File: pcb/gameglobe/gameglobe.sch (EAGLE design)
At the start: 14 parts

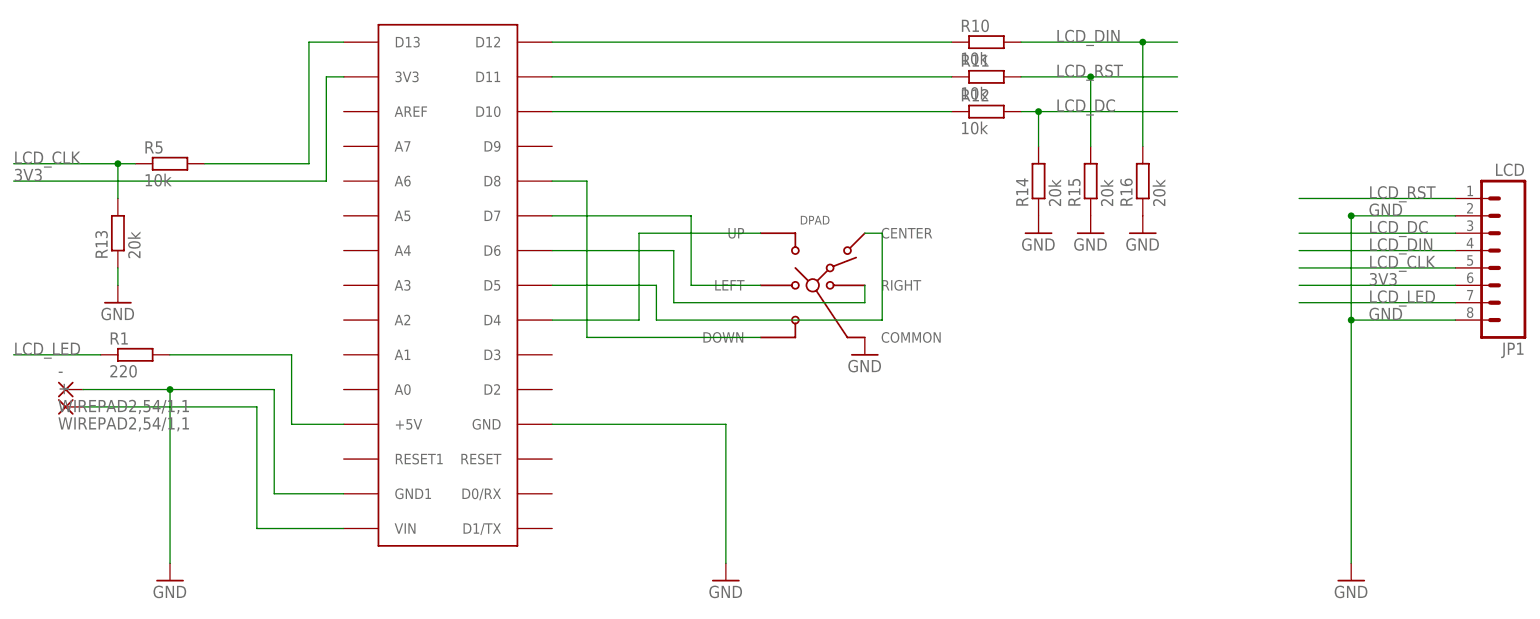
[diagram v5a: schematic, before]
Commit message: Fix and add own arduino Improve silkscreen texts
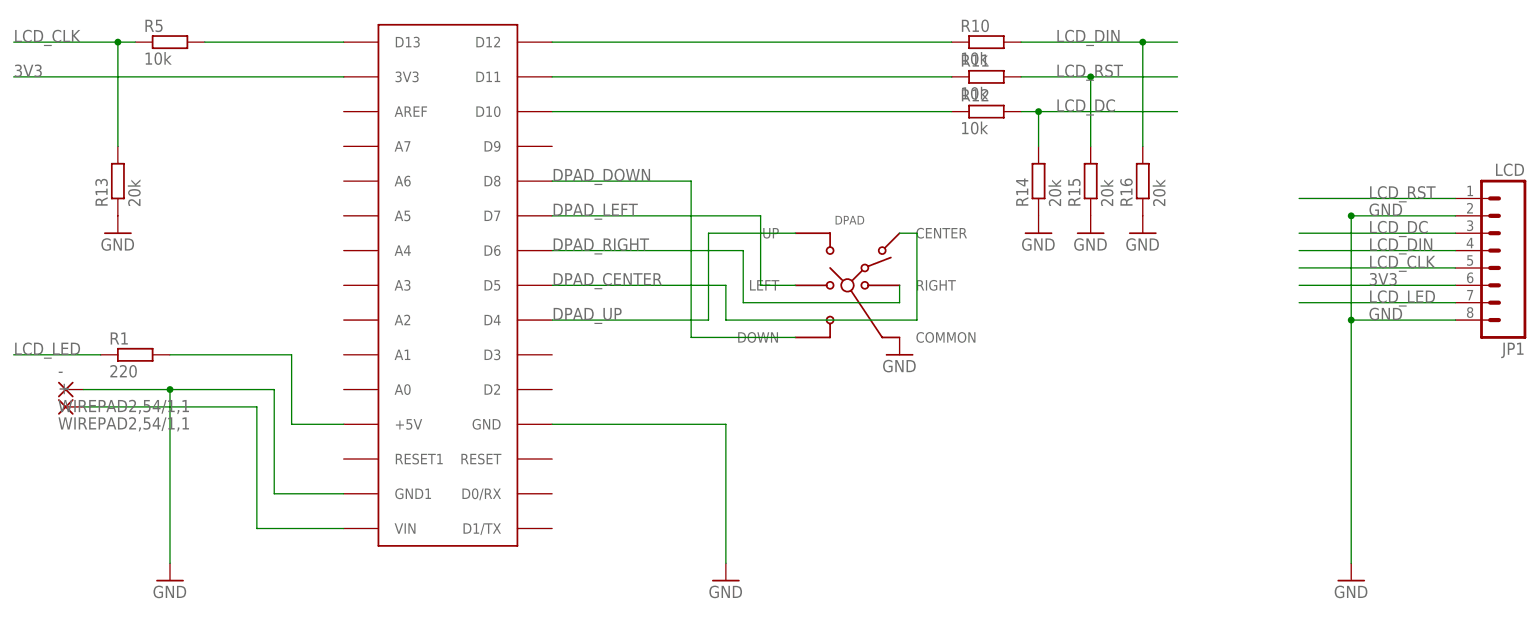
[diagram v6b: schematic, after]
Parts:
- removed U$5: ARDUINONANO, jet-lib:ARDUINONANO
- added ARDUINO_NANO: ARDUINONANO, arduino_nano:ARDUINONANO
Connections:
- removed net N$5: DPAD.DOWN, U$5.D8
- removed net N$6: DPAD.UP, U$5.D4
- new net DPAD_DOWN: ARDUINO_NANO.D8, DPAD.DOWN
- new net DPAD_UP: ARDUINO_NANO.D4, DPAD.UP
- net 3V3: now also ARDUINO_NANO.3V3; no longer U$5.3V3
- net 5V: now also ARDUINO_NANO.+5V; no longer U$5.+5V
- net DPAD_CENTER: now also ARDUINO_NANO.D5; no longer U$5.D5
- net DPAD_LEFT: now also ARDUINO_NANO.D7; no longer U$5.D7
- net DPAD_RIGHT: now also ARDUINO_NANO.D6; no longer U$5.D6
- net GND: now also ARDUINO_NANO.GND, ARDUINO_NANO.GND1; no longer U$5.GND, U$5.GND1
- net N$1: now also ARDUINO_NANO.D13; no longer U$5.D13
- net N$2: now also ARDUINO_NANO.D12; no longer U$5.D12
- net N$3: now also ARDUINO_NANO.D11; no longer U$5.D11
- net N$4: now also ARDUINO_NANO.D10; no longer U$5.D10
- net N$7: now also ARDUINO_NANO.VIN; no longer U$5.VIN
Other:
- moved on the sheet: DPAD, R13, R5
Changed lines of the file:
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@@
 <part name="GND8" library="supply1" deviceset="GND" device=""/>
 <part name="R1" library="resistor" deviceset="R-EU_" device="0411/15" value="220"/>
-<part name="U$5" library="jet-lib" deviceset="ARDUINONANO" device=""/>
+<part name="ARDUINO_NANO" library="arduino_nano" deviceset="ARDUINONANO" device=""/>
 </parts>
 <sheets>
@@
 <instance part="+" gate="G$1" x="-20.32" y="33.02"/>
 <instance part="-" gate="G$1" x="-20.32" y="35.56"/>
-<instance part="R5" gate="G$1" x="-5.08" y="68.58"/>
+<instance part="R5" gate="G$1" x="-5.08" y="86.36"/>
 <instance part="R10" gate="G$1" x="114.3" y="86.36"/>
 <instance part="R11" gate="G$1" x="114.3" y="81.28"/>
 <instance part="R12" gate="G$1" x="114.3" y="76.2"/>
-<instance part="R13" gate="G$1" x="-12.7" y="58.42" rot="R90"/>
+<instance part="R13" gate="G$1" x="-12.7" y="66.04" rot="R90"/>
 <instance part="R14" gate="G$1" x="121.92" y="66.04" rot="R90"/>
 <instance part="R15" gate="G$1" x="129.54" y="66.04" rot="R90"/>
@@
 <instance part="JP1" gate="G$1" x="187.96" y="55.88" rot="R180"/>
 <instance part="GND3" gate="1" x="167.64" y="7.62"/>
-<instance part="GND4" gate="1" x="-12.7" y="48.26"/>
+<instance part="GND4" gate="1" x="-12.7" y="58.42"/>
 <instance part="GND5" gate="1" x="121.92" y="58.42"/>
 <instance part="GND6" gate="1" x="129.54" y="58.42"/>
 <instance part="GND7" gate="1" x="137.16" y="58.42"/>
-<instance part="DPAD" gate="Q$1" x="88.9" y="50.8"/>
-<instance part="GND8" gate="1" x="96.52" y="40.64"/>
+<instance part="DPAD" gate="Q$1" x="93.98" y="50.8"/>
+<instance part="GND8" gate="1" x="101.6" y="40.64"/>
 <instance part="R1" gate="G$1" x="-10.16" y="40.64"/>
-<instance part="U$5" gate="G$1" x="45.72" y="12.7" rot="R180"/>
+<instance part="ARDUINO_NANO" gate="G$1" x="45.72" y="12.7" rot="R180"/>
 </instances>
 <busses>
@@
 <wire x1="7.62" y1="33.02" x2="-17.78" y2="33.02" width="0.1524" layer="91"/>
 <wire x1="7.62" y1="33.02" x2="7.62" y2="15.24" width="0.1524" layer="91"/>
-<pinref part="U$5" gate="G$1" pin="VIN"/>
+<pinref part="ARDUINO_NANO" gate="G$1" pin="VIN"/>
 <wire x1="7.62" y1="15.24" x2="20.32" y2="15.24" width="0.1524" layer="91"/>
 </segment>
@@
 <wire x1="50.8" y1="30.48" x2="76.2" y2="30.48" width="0.1524" layer="91"/>
 <wire x1="76.2" y1="30.48" x2="76.2" y2="10.16" width="0.1524" layer="91"/>
-<pinref part="U$5" gate="G$1" pin="GND"/>
+<pinref part="ARDUINO_NANO" gate="G$1" pin="GND"/>
 </segment>
 <segment>
@@
 <pinref part="-" gate="G$1" pin="P"/>
 <wire x1="10.16" y1="35.56" x2="10.16" y2="20.32" width="0.1524" layer="91"/>
-<pinref part="U$5" gate="G$1" pin="GND1"/>
+<pinref part="ARDUINO_NANO" gate="G$1" pin="GND1"/>
 <wire x1="10.16" y1="20.32" x2="20.32" y2="20.32" width="0.1524" layer="91"/>
 </segment>
@@
 <pinref part="R13" gate="G$1" pin="1"/>
 <pinref part="GND4" gate="1" pin="GND"/>
-<wire x1="-12.7" y1="50.8" x2="-12.7" y2="53.34" width="0.1524" layer="91"/>
 </segment>
 <segment>
@@
 <segment>
 <pinref part="R13" gate="G$1" pin="2"/>
-<wire x1="-12.7" y1="63.5" x2="-12.7" y2="68.58" width="0.1524" layer="91"/>
+<wire x1="-12.7" y1="71.12" x2="-12.7" y2="86.36" width="0.1524" layer="91"/>
 <pinref part="R5" gate="G$1" pin="1"/>
-<wire x1="-12.7" y1="68.58" x2="-10.16" y2="68.58" width="0.1524" layer="91"/>
-<wire x1="-12.7" y1="68.58" x2="-27.94" y2="68.58" width="0.1524" layer="91"/>
-<junction x="-12.7" y="68.58"/>
-<label x="-27.94" y="68.58" size="1.778" layer="95"/>
+<wire x1="-12.7" y1="86.36" x2="-10.16" y2="86.36" width="0.1524" layer="91"/>
+<wire x1="-12.7" y1="86.36" x2="-27.94" y2="86.36" width="0.1524" layer="91"/>
+<junction x="-12.7" y="86.36"/>
+<label x="-27.94" y="86.36" size="1.778" layer="95"/>
 </segment>
 </net>
@@
 </segment>
 <segment>
-<label x="-27.94" y="66.04" size="1.778" layer="95"/>
-<wire x1="17.78" y1="66.04" x2="-27.94" y2="66.04" width="0.1524" layer="91"/>
-<wire x1="17.78" y1="66.04" x2="17.78" y2="81.28" width="0.1524" layer="91"/>
-<pinref part="U$5" gate="G$1" pin="3V3"/>
-<wire x1="17.78" y1="81.28" x2="20.32" y2="81.28" width="0.1524" layer="91"/>
+<label x="-27.94" y="81.28" size="1.778" layer="95"/>
+<wire x1="20.32" y1="81.28" x2="-27.94" y2="81.28" width="0.1524" layer="91"/>
+<pinref part="ARDUINO_NANO" gate="G$1" pin="3V3"/>
 </segment>
 </net>
@@
 <segment>
 <pinref part="R5" gate="G$1" pin="2"/>
-<wire x1="0" y1="68.58" x2="15.24" y2="68.58" width="0.1524" layer="91"/>
-<wire x1="15.24" y1="68.58" x2="15.24" y2="86.36" width="0.1524" layer="91"/>
-<pinref part="U$5" gate="G$1" pin="D13"/>
-<wire x1="15.24" y1="86.36" x2="20.32" y2="86.36" width="0.1524" layer="91"/>
+<wire x1="0" y1="86.36" x2="20.32" y2="86.36" width="0.1524" layer="91"/>
+<pinref part="ARDUINO_NANO" gate="G$1" pin="D13"/>
 </segment>
 </net>
@@
 <segment>
 <pinref part="R10" gate="G$1" pin="1"/>
-<pinref part="U$5" gate="G$1" pin="D12"/>
+<pinref part="ARDUINO_NANO" gate="G$1" pin="D12"/>
 <wire x1="50.8" y1="86.36" x2="109.22" y2="86.36" width="0.1524" layer="91"/>
 </segment>
@@
 <segment>
 <pinref part="R11" gate="G$1" pin="1"/>
-<pinref part="U$5" gate="G$1" pin="D11"/>
+<pinref part="ARDUINO_NANO" gate="G$1" pin="D11"/>
 <wire x1="50.8" y1="81.28" x2="109.22" y2="81.28" width="0.1524" layer="91"/>
 </segment>
@@
 <segment>
 <pinref part="R12" gate="G$1" pin="1"/>
-<pinref part="U$5" gate="G$1" pin="D10"/>
+<pinref part="ARDUINO_NANO" gate="G$1" pin="D10"/>
 <wire x1="50.8" y1="76.2" x2="109.22" y2="76.2" width="0.1524" layer="91"/>
 </segment>
@@
 <segment>
 <pinref part="DPAD" gate="Q$1" pin="LEFT"/>
-<pinref part="U$5" gate="G$1" pin="D7"/>
-<wire x1="50.8" y1="60.96" x2="71.12" y2="60.96" width="0.1524" layer="91"/>
-<wire x1="81.28" y1="50.8" x2="71.12" y2="50.8" width="0.1524" layer="91"/>
-<wire x1="71.12" y1="50.8" x2="71.12" y2="60.96" width="0.1524" layer="91"/>
+<pinref part="ARDUINO_NANO" gate="G$1" pin="D7"/>
+<wire x1="50.8" y1="60.96" x2="81.28" y2="60.96" width="0.1524" layer="91"/>
+<wire x1="86.36" y1="50.8" x2="81.28" y2="50.8" width="0.1524" layer="91"/>
+<wire x1="81.28" y1="50.8" x2="81.28" y2="60.96" width="0.1524" layer="91"/>
+<label x="50.8" y="60.96" size="1.778" layer="95"/>
 </segment>
 </net>
@@
 <segment>
 <pinref part="DPAD" gate="Q$1" pin="RIGHT"/>
-<wire x1="96.52" y1="50.8" x2="96.52" y2="48.26" width="0.1524" layer="91"/>
-<wire x1="96.52" y1="48.26" x2="68.58" y2="48.26" width="0.1524" layer="91"/>
-<wire x1="68.58" y1="48.26" x2="68.58" y2="55.88" width="0.1524" layer="91"/>
-<pinref part="U$5" gate="G$1" pin="D6"/>
-<wire x1="68.58" y1="55.88" x2="50.8" y2="55.88" width="0.1524" layer="91"/>
+<wire x1="101.6" y1="50.8" x2="101.6" y2="48.26" width="0.1524" layer="91"/>
+<wire x1="101.6" y1="48.26" x2="78.74" y2="48.26" width="0.1524" layer="91"/>
+<wire x1="78.74" y1="48.26" x2="78.74" y2="55.88" width="0.1524" layer="91"/>
+<pinref part="ARDUINO_NANO" gate="G$1" pin="D6"/>
+<wire x1="78.74" y1="55.88" x2="50.8" y2="55.88" width="0.1524" layer="91"/>
+<label x="50.8" y="55.88" size="1.778" layer="95"/>
 </segment>
 </net>
@@
 <segment>
 <pinref part="DPAD" gate="Q$1" pin="CENTER"/>
-<wire x1="96.52" y1="58.42" x2="99.06" y2="58.42" width="0.1524" layer="91"/>
-<wire x1="99.06" y1="58.42" x2="99.06" y2="45.72" width="0.1524" layer="91"/>
-<wire x1="99.06" y1="45.72" x2="66.04" y2="45.72" width="0.1524" layer="91"/>
-<wire x1="66.04" y1="45.72" x2="66.04" y2="50.8" width="0.1524" layer="91"/>
-<pinref part="U$5" gate="G$1" pin="D5"/>
-<wire x1="66.04" y1="50.8" x2="50.8" y2="50.8" width="0.1524" layer="91"/>
+<wire x1="101.6" y1="58.42" x2="104.14" y2="58.42" width="0.1524" layer="91"/>
+<wire x1="104.14" y1="58.42" x2="104.14" y2="45.72" width="0.1524" layer="91"/>
+<wire x1="104.14" y1="45.72" x2="76.2" y2="45.72" width="0.1524" layer="91"/>
+<wire x1="76.2" y1="45.72" x2="76.2" y2="50.8" width="0.1524" layer="91"/>
+<pinref part="ARDUINO_NANO" gate="G$1" pin="D5"/>
+<wire x1="76.2" y1="50.8" x2="50.8" y2="50.8" width="0.1524" layer="91"/>
+<label x="50.8" y="50.8" size="1.778" layer="95"/>
 </segment>
 </net>
@@
 <wire x1="-5.08" y1="40.64" x2="12.7" y2="40.64" width="0.1524" layer="91"/>
 <wire x1="12.7" y1="40.64" x2="12.7" y2="30.48" width="0.1524" layer="91"/>
-<pinref part="U$5" gate="G$1" pin="+5V"/>
+<pinref part="ARDUINO_NANO" gate="G$1" pin="+5V"/>
 <wire x1="12.7" y1="30.48" x2="20.32" y2="30.48" width="0.1524" layer="91"/>
 </segment>
 </net>
-<net name="N$5" class="0">
+<net name="DPAD_DOWN" class="0">
 <segment>
 <pinref part="DPAD" gate="Q$1" pin="DOWN"/>
-<wire x1="81.28" y1="43.18" x2="55.88" y2="43.18" width="0.1524" layer="91"/>
-<wire x1="55.88" y1="43.18" x2="55.88" y2="66.04" width="0.1524" layer="91"/>
-<pinref part="U$5" gate="G$1" pin="D8"/>
-<wire x1="55.88" y1="66.04" x2="50.8" y2="66.04" width="0.1524" layer="91"/>
-</segment>
-</net>
-<net name="N$6" class="0">
-<segment>
-<pinref part="U$5" gate="G$1" pin="D4"/>
-<wire x1="50.8" y1="45.72" x2="63.5" y2="45.72" width="0.1524" layer="91"/>
-<wire x1="63.5" y1="45.72" x2="63.5" y2="58.42" width="0.1524" layer="91"/>
+<wire x1="86.36" y1="43.18" x2="71.12" y2="43.18" width="0.1524" layer="91"/>
+<wire x1="71.12" y1="43.18" x2="71.12" y2="66.04" width="0.1524" layer="91"/>
+<pinref part="ARDUINO_NANO" gate="G$1" pin="D8"/>
+<wire x1="71.12" y1="66.04" x2="50.8" y2="66.04" width="0.1524" layer="91"/>
+<label x="50.8" y="66.04" size="1.778" layer="95"/>
+</segment>
+</net>
+<net name="DPAD_UP" class="0">
+<segment>
+<pinref part="ARDUINO_NANO" gate="G$1" pin="D4"/>
+<wire x1="50.8" y1="45.72" x2="73.66" y2="45.72" width="0.1524" layer="91"/>
+<wire x1="73.66" y1="45.72" x2="73.66" y2="58.42" width="0.1524" layer="91"/>
 <pinref part="DPAD" gate="Q$1" pin="UP"/>
-<wire x1="63.5" y1="58.42" x2="81.28" y2="58.42" width="0.1524" layer="91"/>
-</segment>
-</net>
+<wire x1="73.66" y1="58.42" x2="86.36" y2="58.42" width="0.1524" layer="91"/>
+<label x="50.8" y="45.72" size="1.778" layer="95"/>
+</segment>
+</net>
